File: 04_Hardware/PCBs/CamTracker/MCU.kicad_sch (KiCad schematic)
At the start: 42 parts, among them IC1 W25Q128JVSIM, J19 22-28-4034, J20 67996-100HLF, J21 67996-100HLF, J22 USB3076-30-A, Q10 BC817-40,215, Q11 BC817-40,215, U12 RP2040, Y1 ABM8-272-T3

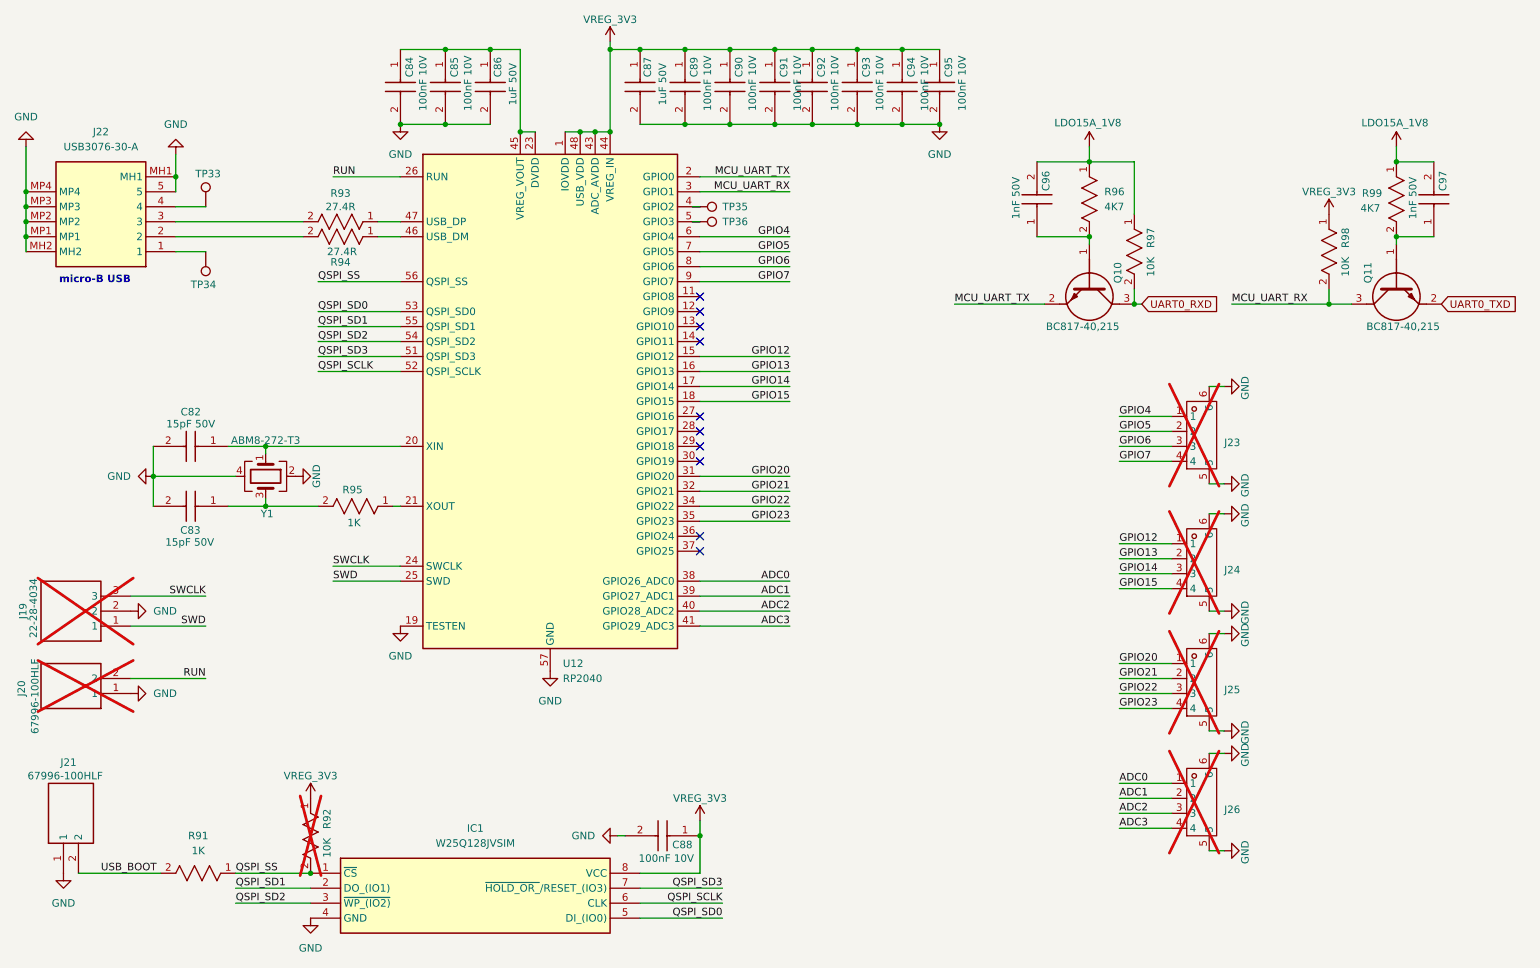
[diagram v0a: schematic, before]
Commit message: feat: Completed Placement v1 in Layout
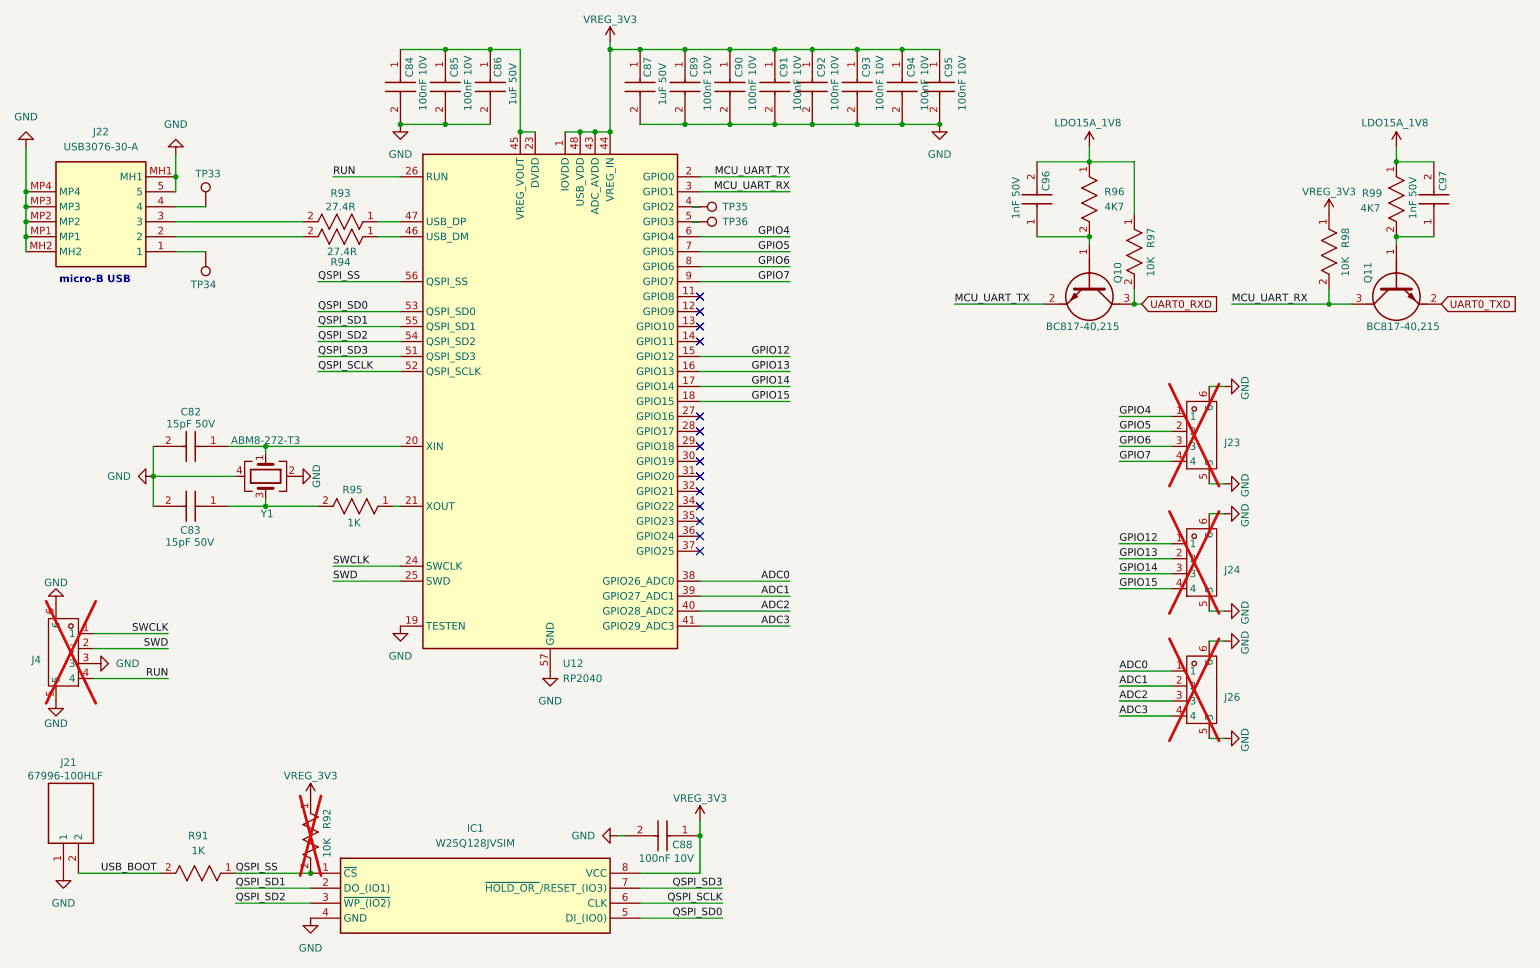
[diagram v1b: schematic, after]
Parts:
- removed J19: 22-28-4034, 000MCLib:HDRV3W66P0X254_1X3_762X249X1042P, symbol 000MCLib:22-28-4034
- removed J20: 67996-100HLF, 000MCLib:HDRV2W67P254_2X1_254X483X858P, symbol 000MCLib:67996-100HLF
- removed J25: ~, 000MCLib:CONN-SMD_1.25-4PLT, symbol 000MCLib:1.25-4P LT
- added J4: ~, 000MCLib:CONN-SMD_1.25-4PLT, symbol 000MCLib:1.25-4P LT
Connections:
- net GND: now also J4.3, J4.5, J4.6
- net RUN: now also J4.4
- net SWCLK: now also J4.1
- net SWD: now also J4.2
- net GPIO20: no longer names the net of U12.31 (GPIO20)
- net GPIO21: no longer names the net of U12.32 (GPIO21)
- net GPIO22: no longer names the net of U12.34 (GPIO22)
- net GPIO23: no longer names the net of U12.35 (GPIO23)
- no-connect marks 10 -> 14
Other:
- moved on the sheet: J26

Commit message: feat(layout): Completed Placement v2
Includes:
- 3V8 DC-DC converter moved to the top layer
- SIM and SD card positions rearranged
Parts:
- removed J24: ~, 000MCLib:CONN-SMD_1.25-4PLT, symbol 000MCLib:1.25-4P LT
- added TP46, TP47, TP48, TP49: TestPoint, TestPoint:TestPoint_Pad_D1.0mm, symbol 000MCLib:TestPoint
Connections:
- net MCU_USB_N: now reaches R94.1, U12.46 (USB_DM)
- net MCU_USB_P: now reaches R93.1, U12.47 (USB_DP)
- net GPIO12: no longer names the net of U12.15 (GPIO12)
- net GPIO12: now also TP46.1
- net GPIO13: no longer names the net of U12.16 (GPIO13)
- net GPIO13: now also TP47.1
- net GPIO14: no longer names the net of U12.17 (GPIO14)
- net GPIO14: now also TP48.1
- net GPIO15: no longer names the net of U12.18 (GPIO15)
- net GPIO15: now also TP49.1
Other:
- moved on the sheet: J23, J26, R93, R94

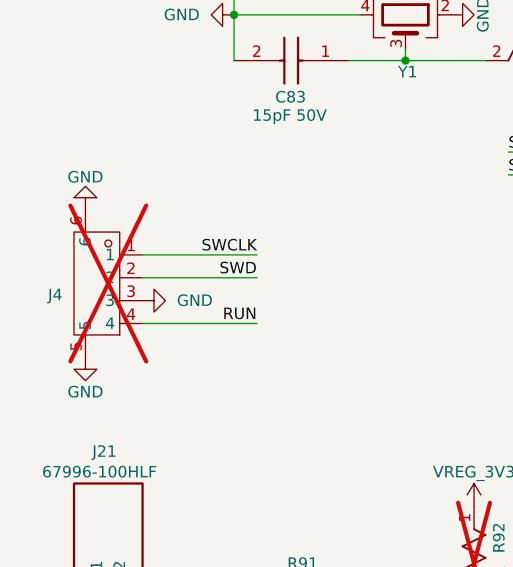
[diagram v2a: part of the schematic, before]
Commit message: feat(layout): Completed Layout Design with new Camera Connectors
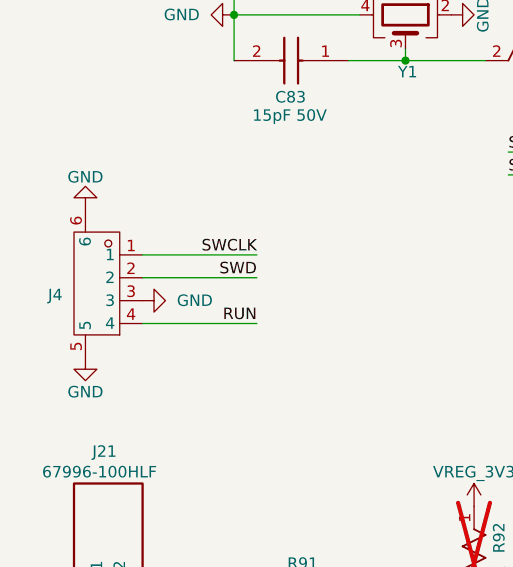
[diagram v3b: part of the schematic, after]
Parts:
- J4: now fitted; now in the parts list
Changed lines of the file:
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@@
 		(unit 1)
 		(exclude_from_sim no)
-		(in_bom no)
+		(in_bom yes)
 		(on_board yes)
-		(dnp yes)
+		(dnp no)
 		(property "Reference" "J4"
 			(at 31.75 127.6351 0)

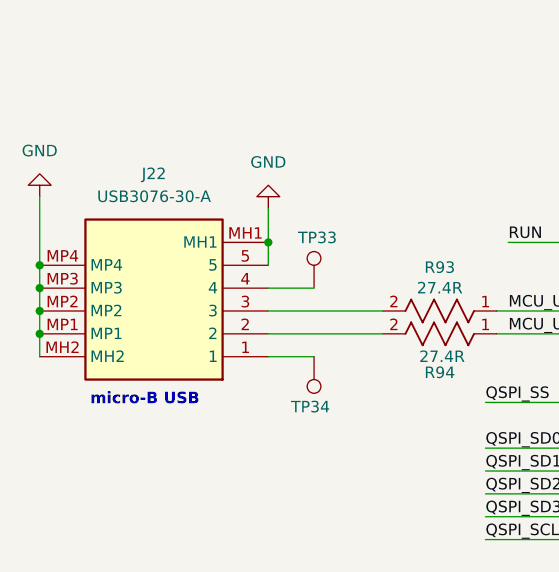
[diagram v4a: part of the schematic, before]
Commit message: feat(PCB): Added TE Connectivity connectors except the SD connector
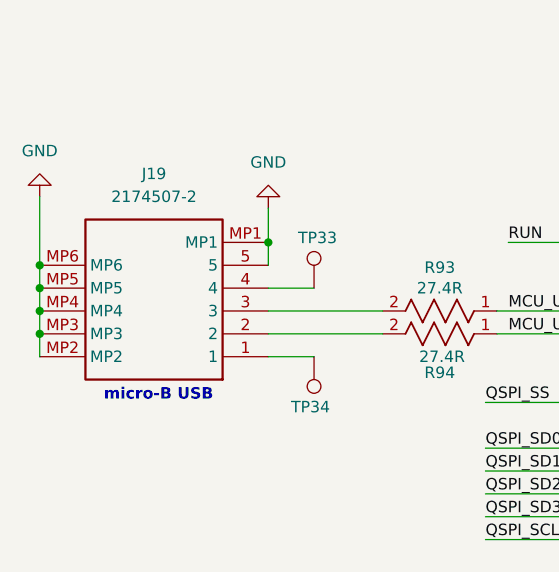
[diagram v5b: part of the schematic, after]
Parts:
- removed J22: USB3076-30-A, 000MCLib:USB307630A, symbol 000MCLib:USB3076-30-A
- added J19: 2174507-2, 000MCLib:21745072, symbol 000MCLib:2174507-2
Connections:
- net GND: now also J19.5, J19.MP1, J19.MP2, J19.MP3, J19.MP4, J19.MP5, J19.MP6
- net at R94.2: now also J19.2
- net at TP33.1: now also J19.4
- net at R93.2: now also J19.3
- net at TP34.1: now also J19.1

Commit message: feat(PCB): Added GPIO IN to SC206E from the MCU
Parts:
- added Q8: BC817-40,215, 000MCLib:BC81740215, symbol 000MCLib:BC817-40,215
- added R28, R47, R48: 10K, 000MCLib:RC0402N_YAG, symbol 000MCLib:RC0402JR-0710KL
- added R50: 0R, 000MCLib:RESC2012X50N, symbol 000MCLib:CRCW08050000Z0EA
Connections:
- net GND: now also Q8.2 (E), R47.1
- net LDO15A_1V8: now also R48.1
- net MCU_OUT: now reaches U12.37 (GPIO25)
- net MCU_OUT: now also R28.2
- new net: Q8.3 (C), R48.2, R50.1
- new net: Q8.1 (B), R28.1, R47.2
- new net GPIO28_MCU_IN: R50.2
- no-connect marks 14 -> 13
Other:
- moved on the sheet: J23, J26

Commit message: feat(PCB): finalize PCB design and generate BOM/Gerbers
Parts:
- R50: Height 0.5 -> (none); Mouser Part Number 71-CRCW0805-0-E3 -> (none); Mouser Price/Stock https://www.mouser.co.uk/ProductDetail/Vishay-Dale/CRCW0805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 -> (none)
